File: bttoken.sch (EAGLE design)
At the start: 41 parts, among them Q1 32k, Q2 10G7A-12.5KHZ, X1 FCI-MICRO-USB

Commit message: Cleaned up stuff
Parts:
- added D1: SFH482, led:SFH482
- added R10: 150, rcl:R-US_R0805
- added R9: 1.5k, rcl:R-US_R0805
- added T1: MMBT3904, transistor:MMBT3904LT1-NPN-SOT23-BEC
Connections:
- removed net N$47: C3P1N.2, U$11.CAP3P
- new net IR_CTL: R9.1, U$1.4
- new net N$12: R9.2, T1.B
- new net N$15: D1.C, T1.C
- new net N$20: CV0.1, CV1.1, CV2.1, CV3.1, CV4.1, CVOUT.1
- new net N$21: C3P1N.1, U$11.CAP3P
- new net N$5: D1.A, R10.2
- new net VCC: R10.1
- net GND: now also T1.E; no longer CV0.1, CV1.1, CV2.1, CV3.1, CV4.1, CVOUT.1
- net N$45: now also C3P1N.2; no longer C3P1N.1
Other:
- note added: "Digital Decoupling DVCCx-GND"
- note added: "IR LED Emitter"
- note removed: "Digital decoupling DVCCx--GND"
- moved on the sheet: C1, C14, C15, C1P, C2, C2P, C3, C3P1N, C4, CV0, CV1, CV2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

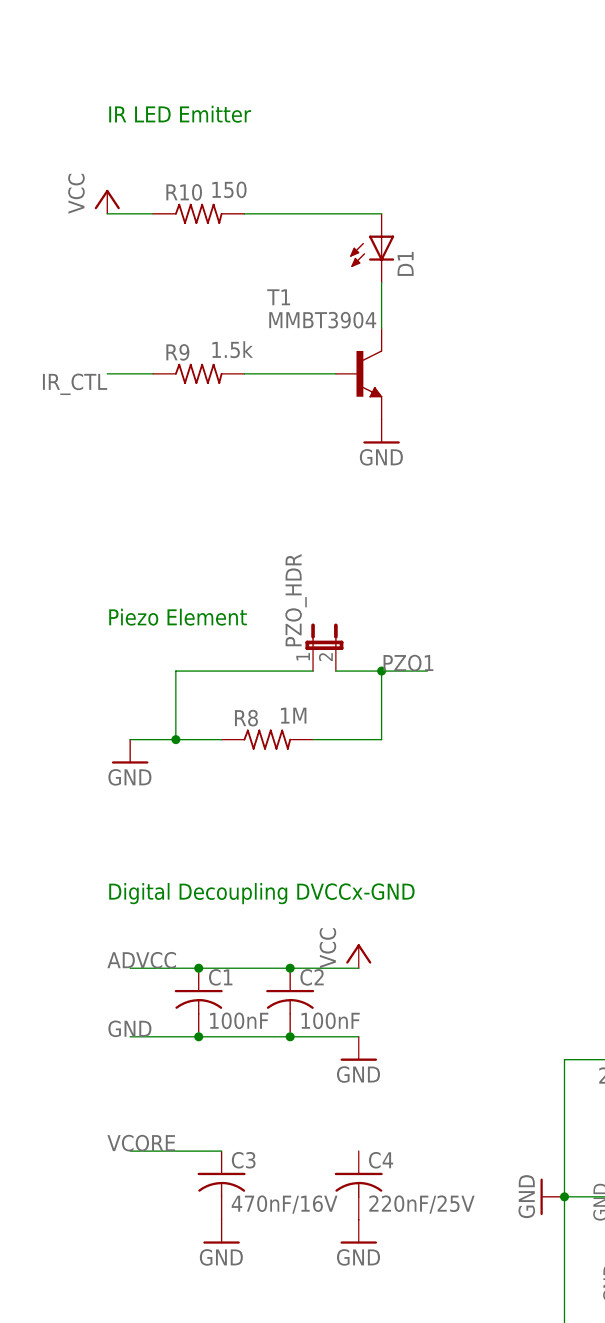
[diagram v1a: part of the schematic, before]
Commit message: Fixed errors warnings and stuff
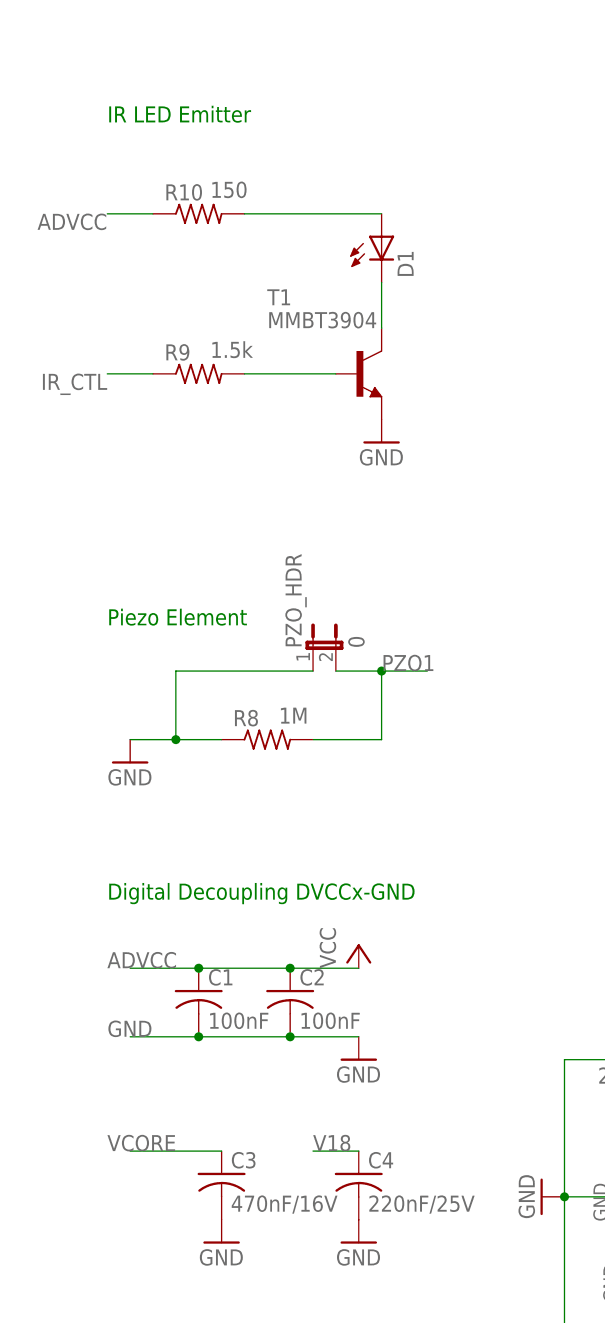
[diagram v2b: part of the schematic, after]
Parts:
- PZO_HDR: value (none) -> 0
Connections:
- removed net N$20: CV0.1, CV1.1, CV2.1, CV3.1, CV4.1, CVOUT.1
- removed net VCC: R10.1
- net ADVCC: now also R10.1
- net GND: now also CV0.1, CV1.1, CV2.1, CV3.1, CV4.1, CVOUT.1
- net V18: now also C4.1

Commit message: New board - Regulator, fix so that eagle doesn't complain etc
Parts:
- added IC1: 0, adafruit:MCP1700TRI
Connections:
- net N$2 renamed CRS_XIN
- net N$3 renamed CRS_XOUT
- net N$4 renamed XT2OUT
- net N$6 renamed RC48
- net N$8 renamed XT2IN
- removed net ADVCC: C1.1, C2.1, C5.1, JP1.1, R1.2, R10.1, U$1.11, U$1.28, U$1.7, U$11.VDD, U$11.VDD2, U$13.P$9
- removed net VCORE: C3.1, U$1.13
- new net DVCC: U$1.11, U$1.28
- new net DVSS: U$1.12, U$1.27
- new net VBAT: IC1.IN
- new net VCC: C1.1, C2.1, C3.1, C5.1, IC1.OUT, JP1.1, R1.2, R10.1, U$1.13, U$1.7, U$11.VDD, U$11.VDD2, U$13.P$9
- net GND: now also IC1.GND; no longer U$1.12, U$1.27
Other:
- note removed: "Analog decoupling AVCC1-GND"
- note removed: "Digital Decoupling DVCCx-GND"
- moved on the sheet: C1, C10, C11, C12, C13, C2, C3, C4, C5, C7, C8, C9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

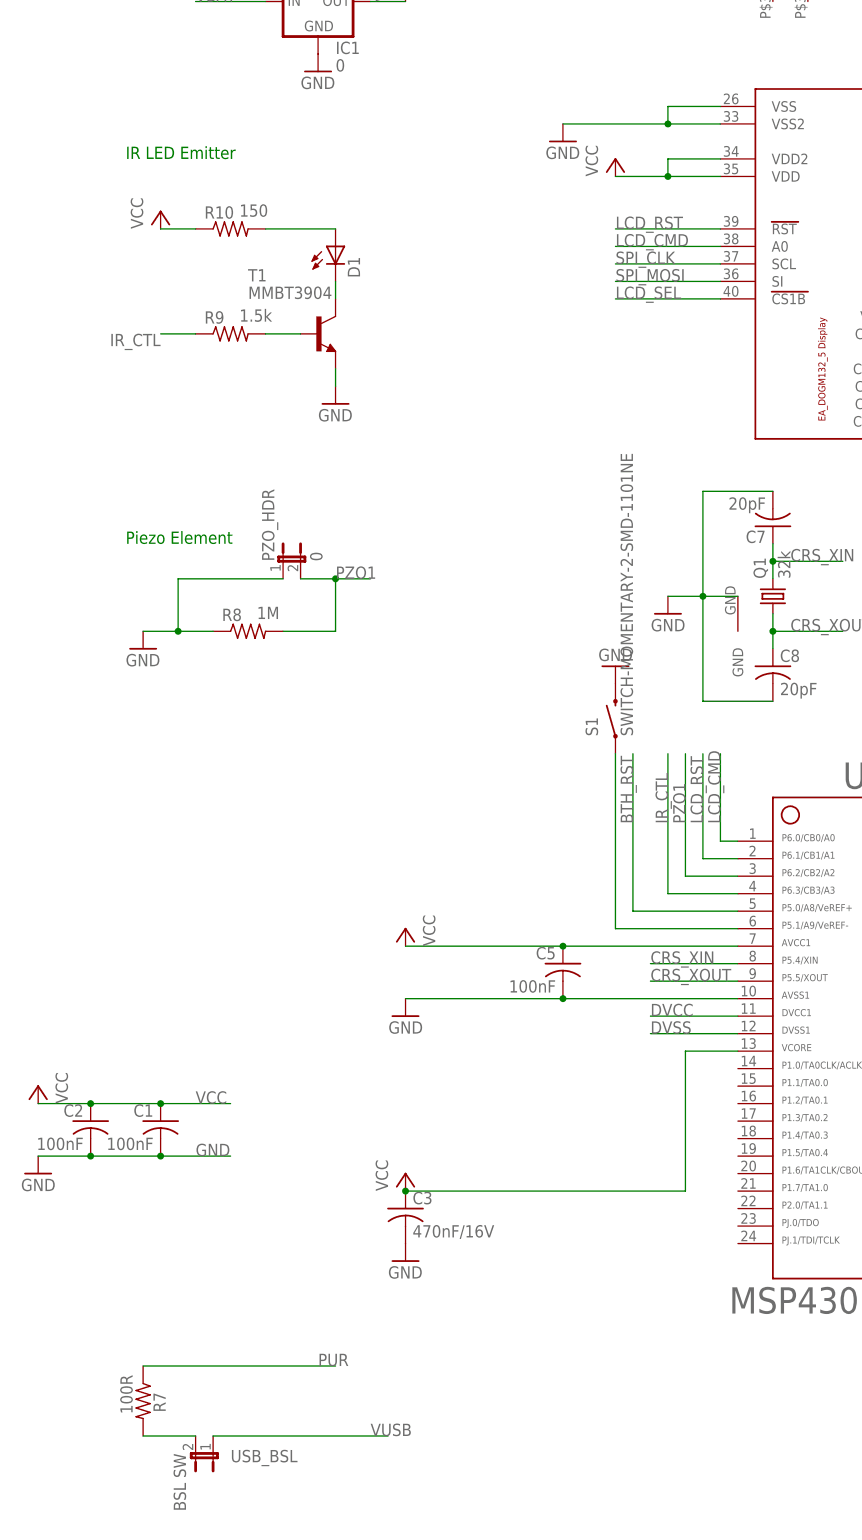
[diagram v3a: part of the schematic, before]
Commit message: Added new charger circuit
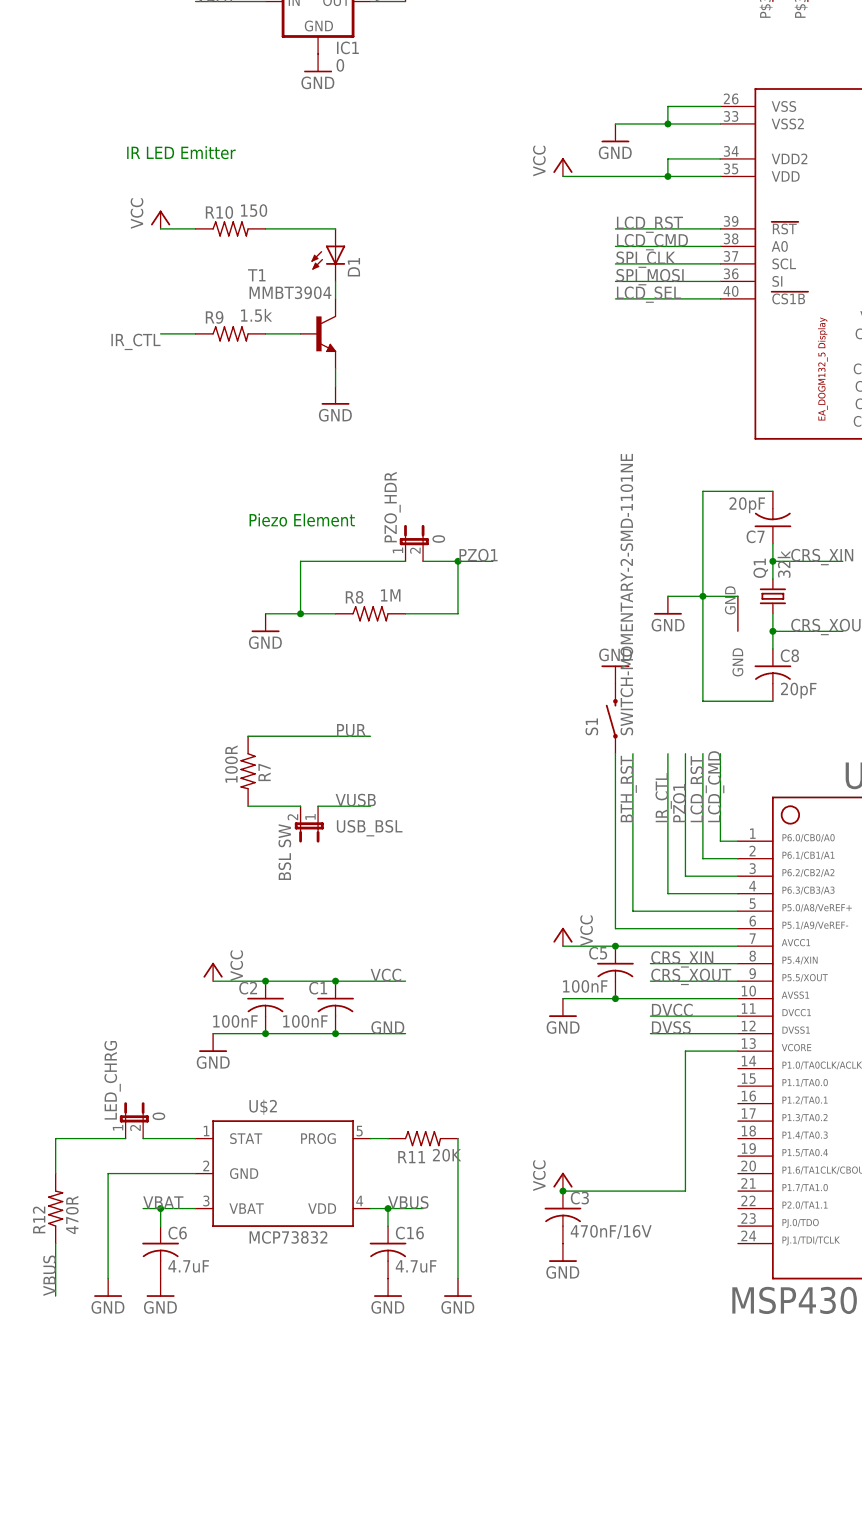
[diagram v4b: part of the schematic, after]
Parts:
- added C16, C6: 4.7uF, rcl:C-USC0805
- added LED_CHRG: 0, jumper:JP1E
- added R11: 20K, rcl:R-US_R0805
- added R12: 470R, rcl:R-US_R0805
- added U$2: MCP73832, DonB:MCP73832
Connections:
- new net N$2: R11.1, U$2.PROG
- new net N$3: LED_CHRG.2, U$2.STAT
- new net N$4: LED_CHRG.1, R12.2
- net GND: now also C16.2, C6.2, R11.2, U$2.GND
- net VBAT: now also C6.1, U$2.VBAT
- net VBUS: now also C16.1, R12.1, U$2.VDD
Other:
- moved on the sheet: C1, C2, C3, C5, PZO_HDR, R7, R8, USB_BSL

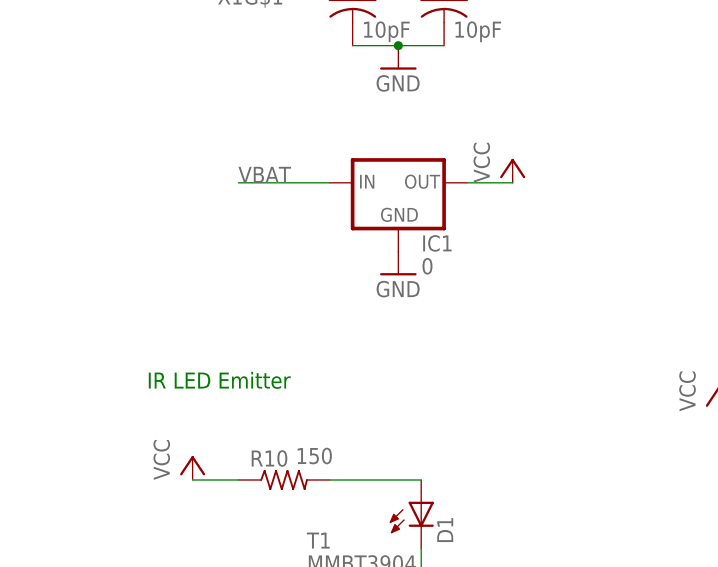
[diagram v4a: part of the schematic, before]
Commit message: Temp CR2032 batt holder until we have a better one
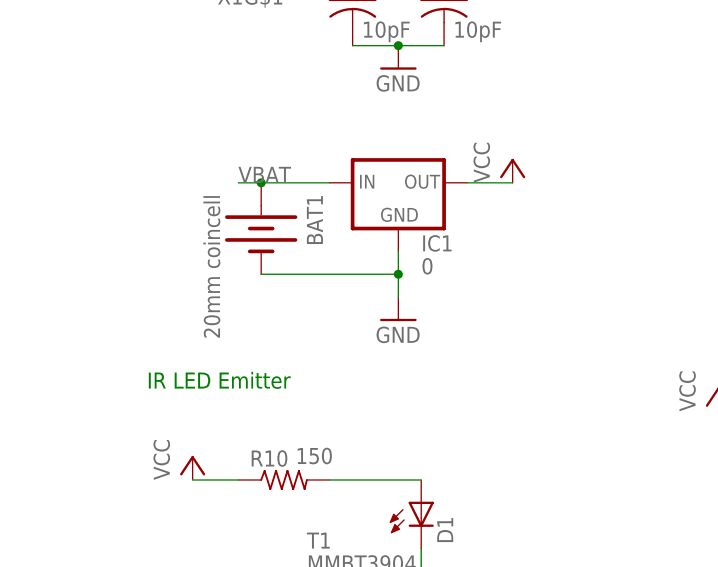
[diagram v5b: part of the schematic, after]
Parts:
- added BAT1: 20mm coincell, SparkFun-Electromechanical:BATTERY20MM_4LEGS
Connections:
- net GND: now also BAT1.-
- net VBAT: now also BAT1.+
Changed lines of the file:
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@@
 <part name="R12" library="rcl" deviceset="R-US_" device="R0805" value="470R"/>
 <part name="LED_CHRG" library="jumper" deviceset="JP1E" device="" value="0"/>
+<part name="BAT1" library="SparkFun-Electromechanical" deviceset="BATTERY" device="20MM_4LEGS" value="20mm coincell"/>
 </parts>
 <sheets>
@@
 <instance part="GND17" gate="1" x="121.92" y="276.86"/>
 <instance part="IC1" gate="1" x="5.08" y="218.44"/>
-<instance part="GND22" gate="1" x="5.08" y="208.28"/>
+<instance part="GND22" gate="1" x="5.08" y="203.2"/>
 <instance part="P+4" gate="VCC" x="40.64" y="48.26"/>
 <instance part="P+5" gate="VCC" x="17.78" y="220.98"/>
@@
 <instance part="R12" gate="G$1" x="-33.02" y="43.18" rot="R90"/>
 <instance part="LED_CHRG" gate="A" x="-22.86" y="55.88"/>
+<instance part="BAT1" gate="G$1" x="-10.16" y="213.36" rot="R270"/>
 </instances>
 <busses>
@@
 <pinref part="IC1" gate="1" pin="GND"/>
 <pinref part="GND22" gate="1" pin="GND"/>
+<wire x1="5.08" y1="205.74" x2="5.08" y2="208.28" width="0.1524" layer="91"/>
+<pinref part="BAT1" gate="G$1" pin="-"/>
+<wire x1="5.08" y1="208.28" x2="5.08" y2="210.82" width="0.1524" layer="91"/>
+<wire x1="-10.16" y1="208.28" x2="5.08" y2="208.28" width="0.1524" layer="91"/>
+<junction x="5.08" y="208.28"/>
 </segment>
 <segment>
@@
 <segment>
 <pinref part="IC1" gate="1" pin="IN"/>
-<wire x1="-2.54" y1="218.44" x2="-12.7" y2="218.44" width="0.1524" layer="91"/>
+<wire x1="-2.54" y1="218.44" x2="-10.16" y2="218.44" width="0.1524" layer="91"/>
 <label x="-12.7" y="218.44" size="1.778" layer="95"/>
-</segment>
-<segment>
+<pinref part="BAT1" gate="G$1" pin="+"/>
+<wire x1="-10.16" y1="218.44" x2="-12.7" y2="218.44" width="0.1524" layer="91"/>
+<junction x="-10.16" y="218.44"/>
+</segment>
+<segment>

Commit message: Checkpoint
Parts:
- BAT1: device SparkFun-Electromechanical:BATTERY20MM_4LEGS -> DonB:BAT-HLD-001
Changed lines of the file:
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@@
 <part name="R12" library="rcl" deviceset="R-US_" device="R0805" value="470R"/>
 <part name="LED_CHRG" library="jumper" deviceset="JP1E" device="" value="0"/>
-<part name="BAT1" library="SparkFun-Electromechanical" deviceset="BATTERY" device="20MM_4LEGS" value="20mm coincell"/>
+<part name="BAT1" library="DonB" deviceset="BAT-HLD-001" device="" value="20mm coincell"/>
 </parts>
 <sheets>
